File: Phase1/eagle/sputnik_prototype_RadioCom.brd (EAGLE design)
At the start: 100 x 100 mm, 98 parts, among them X1 332-44, Y1 32MHz

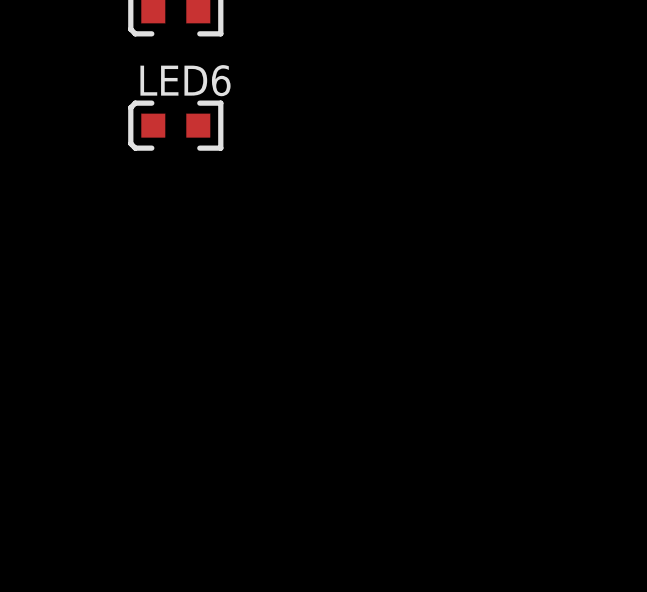
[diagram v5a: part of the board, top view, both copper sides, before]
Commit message: Added more LEDs, filled in LNA values except one inductor which I still need to figure out
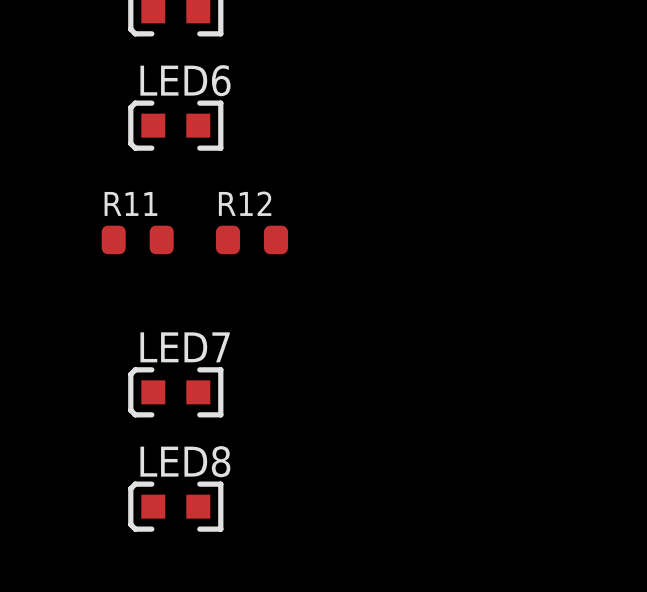
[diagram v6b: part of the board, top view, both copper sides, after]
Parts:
- added LED7, LED8: (no value), psas_c3_team05:LED-0603
- added R11, R12: 1k, rcl_custom:.0603-B-NOSILK
- C23: value (none) -> 1nF
- C24: value (none) -> 10nF
- C43: value (none) -> 100uF
- L8: value (none) -> 150nH
- R1: value (none) -> 250
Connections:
- removed net N$28: LED5.A
- new net N$21: LED7.K, R11.2
- new net N$33: LED8.K, R12.2
- net GND: now also R11.1, R12.1
- net PTC1: now also LED5.A
- net PTC3: now also LED7.A
- net PTC4: now also LED8.A
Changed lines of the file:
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@@
 <element name="L5" library="rcl_custom" package=".0603-B-NOSILK" value="15nH" x="66.04" y="73.66"/>
 <element name="L6" library="rcl_custom" package=".0603-B-NOSILK" value="15nH" x="62.23" y="73.66"/>
-<element name="L8" library="rcl_custom" package=".0603-B-NOSILK" value="" x="96.52" y="77.47"/>
-<element name="R1" library="rcl_custom" package=".0603-B-NOSILK" value="" x="92.71" y="77.47"/>
+<element name="L8" library="rcl_custom" package=".0603-B-NOSILK" value="150nH" x="96.52" y="77.47"/>
+<element name="R1" library="rcl_custom" package=".0603-B-NOSILK" value="250" x="92.71" y="77.47"/>
 <element name="KW0X" library="psas_c3_team05" package="MKW01Z128" value="MKW01Z128" x="38.1" y="36.83">
 <attribute name="MFN" value="NXP" x="38.1" y="36.83" size="1.778" layer="27" display="off"/>
@@
 <attribute name="TP_SIGNAL_NAME" value="" x="49.53" y="60.96" size="1.778" layer="27" display="off"/>
 </element>
-<element name="C23" library="rcl_custom" package=".0402-B-NOSILK" value="" x="29.21" y="78.74"/>
-<element name="C24" library="rcl_custom" package=".0402-B-NOSILK" value="" x="29.21" y="74.93"/>
+<element name="C23" library="rcl_custom" package=".0402-B-NOSILK" value="1nF" x="29.21" y="78.74"/>
+<element name="C24" library="rcl_custom" package=".0402-B-NOSILK" value="10nF" x="29.21" y="74.93"/>
 <element name="C25" library="rcl_custom" package=".0402-B-NOSILK" value="1nF" x="29.21" y="71.12"/>
-<element name="C43" library="rcl" package="CT6032" value="" x="33.02" y="64.77"/>
+<element name="C43" library="rcl" package="CT6032" value="100uF" x="33.02" y="64.77"/>
 <element name="L7" library="rcl_custom" package=".0402-B-NOSILK" value="" x="29.21" y="58.42"/>
 <element name="U$9" library="psas_c3_team05" package="LD39200" value="LD39200" x="77.47" y="46.99"/>
@@
 <element name="R8" library="rcl_custom" package=".0603-B-NOSILK" value="1k" x="2.54" y="-59.69"/>
 <element name="LED5" library="psas_c3_team05" package="LED-0603" value="" x="3.81" y="-73.66">
-<attribute name="GREEN" value="" x="3.81" y="-68.58" size="1.778" layer="27" display="off"/>
+<attribute name="ORANGE" value="" x="3.81" y="-68.58" size="1.778" layer="27" display="off"/>
 </element>
 <element name="R9" library="rcl_custom" package=".0603-B-NOSILK" value="1k" x="2.54" y="-68.58"/>
 <element name="LED6" library="psas_c3_team05" package="LED-0603" value="" x="3.81" y="-77.47">
-<attribute name="GREEN" value="" x="3.81" y="-77.47" size="1.778" layer="27" display="off"/>
+<attribute name="ORANGE" value="" x="3.81" y="-77.47" size="1.778" layer="27" display="off"/>
 </element>
 <element name="R10" library="rcl_custom" package=".0603-B-NOSILK" value="1k" x="6.35" y="-68.58"/>
+<element name="LED7" library="psas_c3_team05" package="LED-0603" value="" x="3.81" y="-86.36">
+<attribute name="ORANGE" value="" x="3.81" y="-81.28" size="1.778" layer="27" display="off"/>
+</element>
+<element name="R11" library="rcl_custom" package=".0603-B-NOSILK" value="1k" x="2.54" y="-81.28"/>
+<element name="LED8" library="psas_c3_team05" package="LED-0603" value="" x="3.81" y="-90.17">
+<attribute name="ORANGE" value="" x="3.81" y="-90.17" size="1.778" layer="27" display="off"/>
+</element>
+<element name="R12" library="rcl_custom" package=".0603-B-NOSILK" value="1k" x="6.35" y="-81.28"/>
 </elements>
 <signals>
@@
 <contactref element="R9" pad="1"/>
 <contactref element="R10" pad="1"/>
+<contactref element="R11" pad="1"/>
+<contactref element="R12" pad="1"/>
 <wire x1="95.72" y1="69.85" x2="95.72" y2="73.66" width="0" layer="19" extent="1-1"/>
 <wire x1="91.91" y1="69.85" x2="95.72" y2="69.85" width="0" layer="19" extent="1-1"/>
@@
 <wire x1="1.74" y1="-68.58" x2="1.74" y2="-59.69" width="0" layer="19" extent="1-1"/>
 <wire x1="5.55" y1="-68.58" x2="1.74" y2="-68.58" width="0" layer="19" extent="1-1"/>
+<wire x1="1.74" y1="-81.28" x2="1.74" y2="-68.58" width="0" layer="19" extent="1-1"/>
+<wire x1="5.55" y1="-81.28" x2="1.74" y2="-81.28" width="0" layer="19" extent="1-1"/>
 </signal>
 <signal name="V+">
@@
 <contactref element="JP2" pad="3"/>
 <contactref element="X1" pad="5"/>
+<contactref element="LED5" pad="A"/>
 <wire x1="27.94" y1="3.81" x2="41.9778" y2="38.08" width="0" layer="19" extent="1-1"/>
 <wire x1="5.86" y1="-14.97" x2="27.94" y2="3.81" width="0" layer="19" extent="1-1"/>
+<wire x1="4.56" y1="-73.66" x2="5.86" y2="-14.97" width="0" layer="19" extent="1-1"/>
 </signal>
 <signal name="PTC2">
@@
 <contactref element="JP2" pad="5"/>
 <contactref element="X1" pad="7"/>
-<wire x1="33.02" y1="3.81" x2="41.9778" y2="39.08" width="0" layer="19" extent="1-1"/>
-<wire x1="7.86" y1="-14.97" x2="33.02" y2="3.81" width="0" layer="19" extent="1-1"/>
+<contactref element="LED7" pad="A"/>
+<wire x1="7.86" y1="-14.97" x2="4.56" y2="-86.36" width="0" layer="19" extent="1-1"/>
+<wire x1="33.02" y1="3.81" x2="7.86" y2="-14.97" width="0" layer="19" extent="1-1"/>
+<wire x1="41.9778" y1="39.08" x2="33.02" y2="3.81" width="0" layer="19" extent="1-1"/>
 </signal>
 <signal name="PTC4">
@@
 <contactref element="JP2" pad="6"/>
 <contactref element="X1" pad="8"/>
-<wire x1="35.56" y1="3.81" x2="41.9778" y2="37.58" width="0" layer="19" extent="1-1"/>
-<wire x1="7.86" y1="-12.97" x2="35.56" y2="3.81" width="0" layer="19" extent="1-1"/>
+<contactref element="LED8" pad="A"/>
+<wire x1="7.86" y1="-12.97" x2="4.56" y2="-90.17" width="0" layer="19" extent="1-1"/>
+<wire x1="35.56" y1="3.81" x2="7.86" y2="-12.97" width="0" layer="19" extent="1-1"/>
+<wire x1="41.9778" y1="37.58" x2="35.56" y2="3.81" width="0" layer="19" extent="1-1"/>
 </signal>
 <signal name="PTC5">
@@
 <wire x1="3.34" y1="-68.58" x2="3.06" y2="-73.66" width="0" layer="19" extent="1-1"/>
 </signal>
-<signal name="N$28">
-<contactref element="LED5" pad="A"/>
-</signal>
 <signal name="N$29">
 <contactref element="LED6" pad="K"/>
@@
 <contactref element="LED6" pad="A"/>
 </signal>
+<signal name="N$21">
+<contactref element="LED7" pad="K"/>
+<contactref element="R11" pad="2"/>
+<wire x1="3.34" y1="-81.28" x2="3.06" y2="-86.36" width="0" layer="19" extent="1-1"/>
+</signal>
+<signal name="N$33">
+<contactref element="LED8" pad="K"/>
+<contactref element="R12" pad="2"/>
+<wire x1="7.15" y1="-81.28" x2="3.06" y2="-90.17" width="0" layer="19" extent="1-1"/>
+</signal>
 </signals>

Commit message: Added RESET (RF) line to PTE2 GPIO. Waiting on LNA component values from MAACOM.
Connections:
- removed net SOMETHING: KW0X.48
- net DIO0: now also KW0X.48
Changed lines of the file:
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@@
 <wire x1="41.9778" y1="35.08" x2="78.72" y2="46.805" width="0" layer="19" extent="1-1"/>
-</signal>
-<signal name="SOMETHING">
-<contactref element="KW0X" pad="48"/>
 </signal>
 <signal name="LNA_EN">
@@
 <contactref element="KW0X" pad="49"/>
 <contactref element="TP16" pad="TP"/>
+<contactref element="KW0X" pad="48"/>
+<wire x1="34.2222" y1="37.58" x2="34.2222" y2="37.08" width="0" layer="19" extent="1-1"/>
 <wire x1="3.81" y1="16.51" x2="34.2222" y2="37.08" width="0" layer="19" extent="1-1"/>
 </signal>

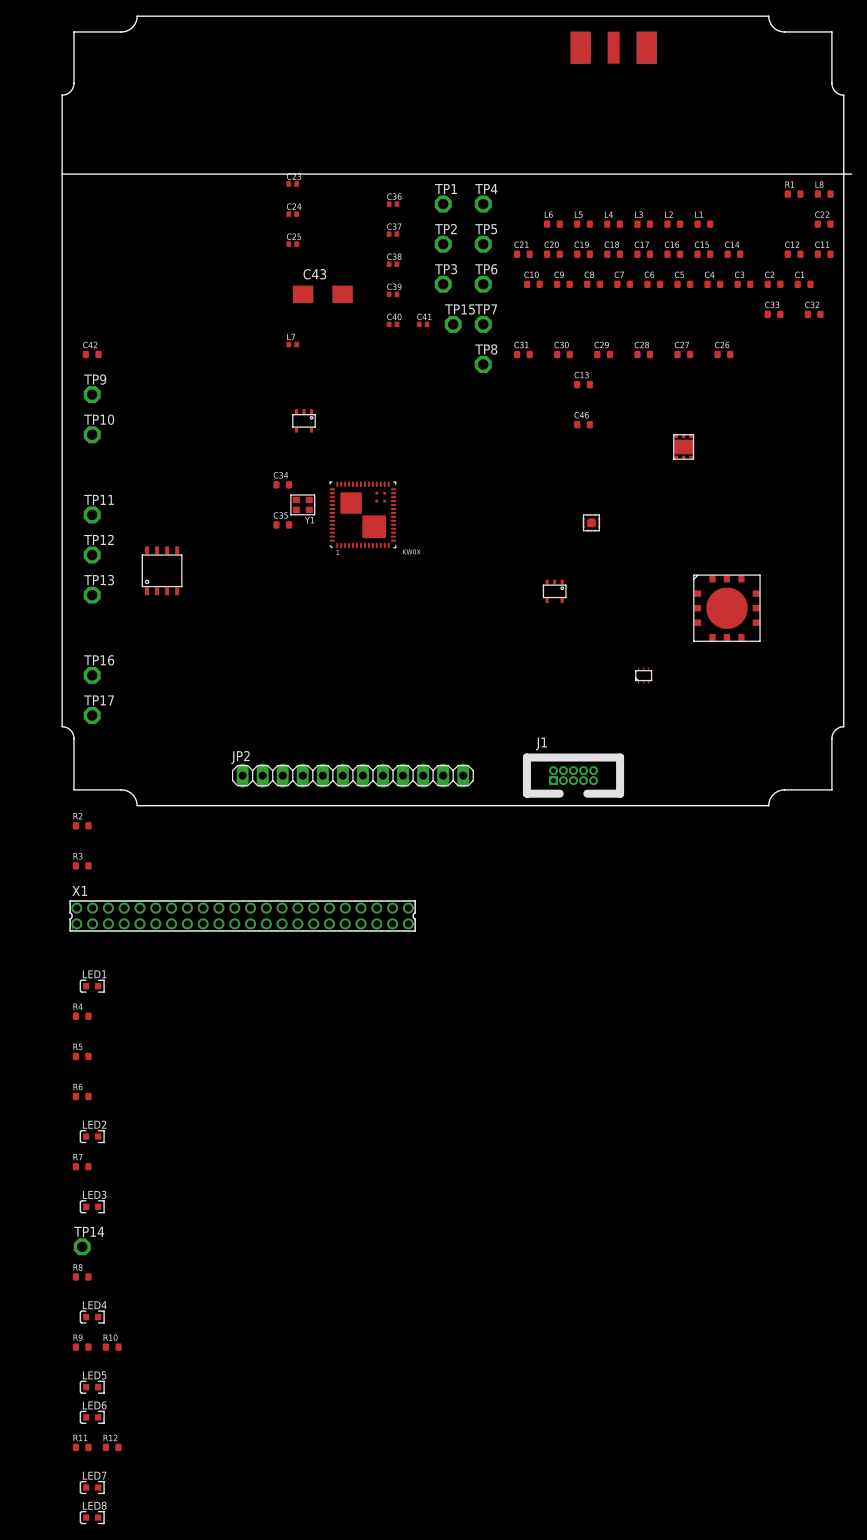
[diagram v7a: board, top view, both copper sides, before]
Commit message: OCD fixes on SPI flash. Made single nets on GPIO that aren't connected. Made new connectors for OreSat connector and RF connector and added them. Updates to a library part for the outline. Made it 4 layers, because that's what it's gonna be. Ooo the excitement, this is starting to look like a thing. Still waiting for final placement data from Jeremy before the connectors can be finalized.
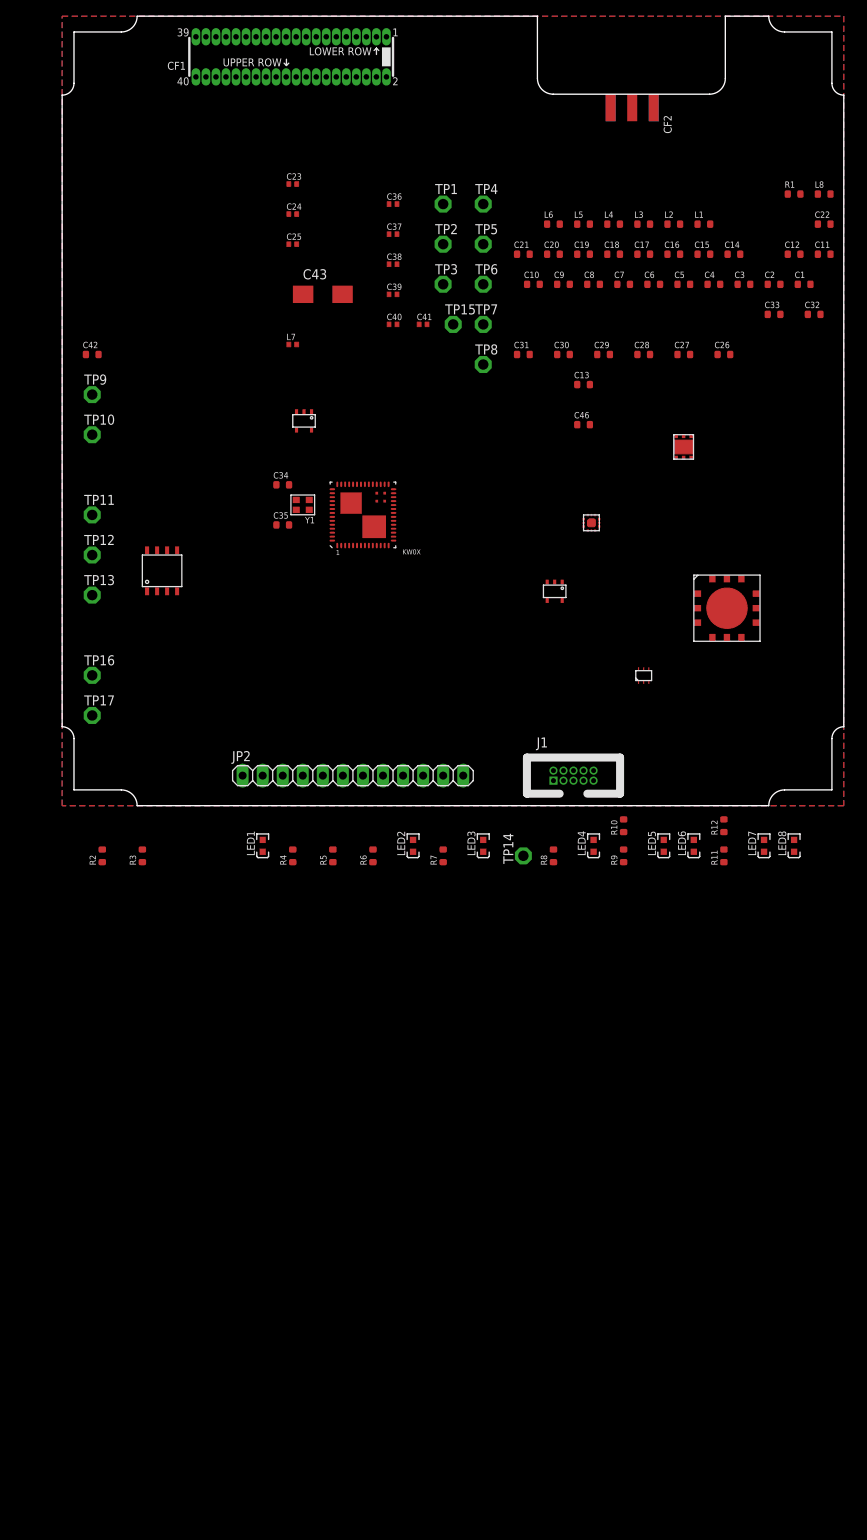
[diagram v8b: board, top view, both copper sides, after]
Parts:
- removed SMA: SMAJ716-ND, psas_c3_team05:SMAJ716-ND
- removed X1: 332-44, con-garry:332-44
- added CF1: ORESAT-CONNECTOR-40PIN, oresat-eagle:HARWIN-ARCHER-M50-3202045
- added CF2: CON-MCX-LINX, oresat-eagle:CON-MCX-LINX-CONMCX003.062
- added U$35: (no value), oresat-eagle:ORESAT-CARD-RF-V0.3
- moved LED8 123.1 mm to (92.7, -5.08), turned to 90 degrees
- moved LED7 117.7 mm to (88.9, -5.08), turned to 90 degrees
- moved R11 110.5 mm to (83.8, -6.35), turned to 90 degrees
- moved R12 110.5 mm to (83.8, -2.54), turned to 90 degrees
- moved LED6 105.1 mm to (80.0, -5.08), turned to 90 degrees
- moved LED5 99.7 mm to (76.2, -5.08), turned to 90 degrees
- moved R9 92.6 mm to (71.1, -6.35), turned to 90 degrees
- moved R10 92.5 mm to (71.1, -2.54), turned to 90 degrees
- moved LED4 87.2 mm to (67.3, -5.08), turned to 90 degrees
- moved R8 80.1 mm to (62.2, -6.35), turned to 90 degrees
- moved TP14 74.7 mm to (58.4, -6.35), turned to 90 degrees
- moved LED3 67.4 mm to (53.3, -5.08), turned to 90 degrees
- moved R7 60.3 mm to (48.3, -6.35), turned to 90 degrees
- moved LED2 54.8 mm to (44.5, -5.08), turned to 90 degrees
- moved R6 47.8 mm to (39.4, -6.35), turned to 90 degrees
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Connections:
- net !WP renamed PTE1
- removed net 3.3V1: LED2.A
- removed net N$32: LED6.A
- new net PTE0: KW0X.32
- net !HOLD: no longer KW0X.32
- net 3.3V: no longer TP5.TP
- net GND: now also CF1.P$37, CF1.P$38, CF1.P$39, CF1.P$40, CF2.SHIELD1, CF2.SHIELD2, CF2.SHIELD3, CF2.SHIELD4; no longer SMA.GND1, SMA.GND2, SMA.GND3, SMA.GND4, X1.21, X1.22
- net N$11: now also TP5.TP
- net N$30: now also CF2.CENTER; no longer SMA.P$3
- net PTB17: now also CF1.P$2; no longer X1.4
- net PTB2: now also CF1.P$1; no longer X1.3
- net PTC1: now also CF1.P$3; no longer X1.5
- net PTC2: now also CF1.P$4, LED6.A; no longer X1.6
- net PTC3: now also CF1.P$5; no longer X1.7
- net PTC4: now also CF1.P$6; no longer X1.8
- net PTC5: now also CF1.P$7; no longer X1.9
- net PTC6: now also CF1.P$8; no longer X1.10
- net PTC7: now also CF1.P$9; no longer X1.11
- net PTD0: now also CF1.P$10; no longer X1.12
- net PTE16: now also CF1.P$11; no longer X1.13
- net PTE17: now also CF1.P$12; no longer X1.14
- net PTE18: now also CF1.P$13; no longer X1.15
- net PTE19: now also CF1.P$14; no longer X1.16
- net UART0_RX: now also CF1.P$17, CF1.P$18; no longer X1.19, X1.20
- net UART0_TX: now also CF1.P$15, CF1.P$16; no longer X1.17, X1.18
- net V+: now also CF1.P$33, CF1.P$34, CF1.P$35, CF1.P$36; no longer X1.1, X1.2
- net VBIAS: now also LED2.A
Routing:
- added copper zone on layer 1, net GND
- added copper zone on layer 15, net GND
- added copper zone on layer 16, net GND
- added copper zone on layer 2, net GND
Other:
- board size 100 x 100 mm -> 99 x 100 mm
